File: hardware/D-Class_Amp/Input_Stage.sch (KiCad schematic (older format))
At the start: 19 parts, among them U201 LM324

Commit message: Added potentiometer to input gain stage, assigned all input footprints
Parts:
- removed R208: 39k, Resistor_SMD:R_0805_2012Metric_Pad1.20x1.40mm_HandSolder, symbol Device:R
- added RV201: 50k, Potentiometer_THT:Potentiometer_Vishay_T73YP_Vertical, symbol Device:R_POT
- added TP201: DC_Offset, TestPoint:TestPoint_THTPad_D2.0mm_Drill1.0mm, symbol Connector:TestPoint
- added TP202: Gain_Stage, TestPoint:TestPoint_THTPad_D2.0mm_Drill1.0mm, symbol Connector:TestPoint
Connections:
- net C_OUT: now also RV201.3
- net at C203.1, R201.2, R202.2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: now also TP201.1
- net at U201.10 (+): now also RV201.2, TP202.1
- no-connect marks 0 -> 1
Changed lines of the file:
@@
 	-1   0    0    -1
 $EndComp
-$Comp
-L Device:R R208
-U 1 1 610F6964
-P 3650 4400
-F 0 "R208" H 3580 4354 50  0000 R CNN
-F 1 "39k" H 3580 4445 50  0000 R CNN
-F 2 "Resistor_SMD:R_0805_2012Metric_Pad1.20x1.40mm_HandSolder" V 3580 4400 50  0001 C CNN
-F 3 "~" H 3650 4400 50  0001 C CNN
-	1    3650 4400
-	-1   0    0    -1
-$EndComp
-Wire Wire Line
-	3650 4600 3650 4550
 Connection ~ 3650 4600
 Wire Wire Line
 	3650 4600 3750 4600
-Wire Wire Line
-	3650 4250 3650 4200
-Wire Wire Line
-	3650 4200 2950 4200
 Wire Wire Line
 	2950 4200 2950 4500
@@
 $EndComp
 Wire Wire Line
-	2250 3200 2600 3200
+	2250 3200 2550 3200
+$Comp
+L Device:R_POT RV201
+U 1 1 61134898
+P 3650 4400
+F 0 "RV201" H 3580 4446 50  0000 R CNN
+F 1 "50k" H 3580 4355 50  0000 R CNN
+F 2 "Potentiometer_THT:Potentiometer_Vishay_T73YP_Vertical" H 3650 4400 50  0001 C CNN
+F 3 "~" H 3650 4400 50  0001 C CNN
+	1    3650 4400
+	1    0    0    -1
+$EndComp
+Wire Wire Line
+	3650 4600 3650 4550
+NoConn ~ 3650 4250
+Wire Wire Line
+	3850 4200 3850 4400
+Wire Wire Line
+	3850 4400 3800 4400
+Wire Wire Line
+	2950 4200 3850 4200
+$Comp
+L Connector:TestPoint TP202
+U 1 1 61142C7C
+P 3850 4150
+F 0 "TP202" H 3908 4268 50  0000 L CNN
+F 1 "Gain_Stage" H 3908 4177 50  0000 L CNN
+F 2 "TestPoint:TestPoint_THTPad_D2.0mm_Drill1.0mm" H 4050 4150 50  0001 C CNN
+F 3 "~" H 4050 4150 50  0001 C CNN
+	1    3850 4150
+	1    0    0    -1
+$EndComp
+Wire Wire Line
+	3850 4200 3850 4150
+Connection ~ 3850 4200
+$Comp
+L Connector:TestPoint TP201
+U 1 1 611488F4
+P 2550 2900
+F 0 "TP201" H 2608 3018 50  0000 L CNN
+F 1 "DC_Offset" H 2600 3100 50  0000 L CNN
+F 2 "TestPoint:TestPoint_THTPad_D2.0mm_Drill1.0mm" H 2750 2900 50  0001 C CNN
+F 3 "~" H 2750 2900 50  0001 C CNN
+	1    2550 2900
+	1    0    0    -1
+$EndComp
+Wire Wire Line
+	2550 2900 2550 3200
+Connection ~ 2550 3200
+Wire Wire Line
+	2550 3200 2600 3200
 $EndSCHEMATC

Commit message: Started input stage layout
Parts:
- R201, R206: footprint (none) -> Resistor_SMD:R_0805_2012Metric_Pad1.20x1.40mm_HandSolder
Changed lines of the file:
@@
 F 0 "R206" H 2180 3446 50  0000 R CNN
 F 1 "100k" H 2180 3355 50  0000 R CNN
-F 2 "" V 2180 3400 50  0001 C CNN
+F 2 "Resistor_SMD:R_0805_2012Metric_Pad1.20x1.40mm_HandSolder" V 2180 3400 50  0001 C CNN
 F 3 "~" H 2250 3400 50  0001 C CNN
 	1    2250 3400
@@
 F 0 "R201" H 2180 3046 50  0000 R CNN
 F 1 "100k" H 2180 2955 50  0000 R CNN
-F 2 "" V 2180 3000 50  0001 C CNN
+F 2 "Resistor_SMD:R_0805_2012Metric_Pad1.20x1.40mm_HandSolder" V 2180 3000 50  0001 C CNN
 F 3 "~" H 2250 3000 50  0001 C CNN
 	1    2250 3000

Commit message: Updated and fixed the input filter schematic
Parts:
- removed R206: 100k, Resistor_SMD:R_0805_2012Metric_Pad1.20x1.40mm_HandSolder, symbol Device:R
- added JP1: Filter_Bypass, Jumper:SolderJumper-2_P1.3mm_Open_TrianglePad1.0x1.5mm, symbol Jumper:SolderJumper_2_Open
- C201: value 100n -> 120n
- C202: value 100n -> 750n
- C207: value 100n -> 2.2u
- C208: value 100n -> 1.2u
- R202: value 5.6k -> 4.3k
- R203: value 8.2k -> 5.6k
- R204: value 5.6k -> 1.5k
- R205: value 8.2k -> 2.4k
- R210: value 8.2k -> 15k
- RV201: value 50k -> 20k
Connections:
- net +2V5: now also R201.1
- net +5V: no longer R201.1
- net A_OUT: now also U201.2 (-); no longer U201.3 (+)
- net B_OUT: now also U201.10 (+), U201.6 (-); no longer U201.5 (+), U201.9 (-)
- net C_OUT: now also JP1.2 (B)
- net FILT_OUT: now also U201.13 (-), JP1.1 (A); no longer U201.12 (+)
- net at C204.2, R203.1: now also U201.3 (+); no longer U201.2 (-)
- net at C205.2, R205.1: now also U201.5 (+); no longer U201.6 (-)
- net at RV201.2, TP202.1: now also U201.9 (-); no longer U201.10 (+)
- net at C208.1, R210.2: now also U201.12 (+); no longer U201.13 (-)
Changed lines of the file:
@@
 P 2750 3200
 F 0 "R202" V 2543 3200 50  0000 C CNN
-F 1 "5.6k" V 2634 3200 50  0000 C CNN
+F 1 "4.3k" V 2634 3200 50  0000 C CNN
 F 2 "Resistor_SMD:R_0805_2012Metric_Pad1.20x1.40mm_HandSolder" V 2680 3200 50  0001 C CNN
 F 3 "~" H 2750 3200 50  0001 C CNN
@@
 P 3150 3200
 F 0 "R203" V 2943 3200 50  0000 C CNN
-F 1 "8.2k" V 3034 3200 50  0000 C CNN
+F 1 "5.6k" V 3034 3200 50  0000 C CNN
 F 2 "Resistor_SMD:R_0805_2012Metric_Pad1.20x1.40mm_HandSolder" V 3080 3200 50  0001 C CNN
 F 3 "~" H 3150 3200 50  0001 C CNN
@@
 P 3150 2800
 F 0 "C201" V 2898 2800 50  0000 C CNN
-F 1 "100n" V 2989 2800 50  0000 C CNN
+F 1 "120n" V 2989 2800 50  0000 C CNN
 F 2 "Capacitor_SMD:C_0805_2012Metric_Pad1.18x1.45mm_HandSolder" H 3188 2650 50  0001 C CNN
 F 3 "~" H 3150 2800 50  0001 C CNN
@@
 P 5300 3200
 F 0 "R204" V 5093 3200 50  0000 C CNN
-F 1 "5.6k" V 5184 3200 50  0000 C CNN
+F 1 "1.5k" V 5184 3200 50  0000 C CNN
 F 2 "Resistor_SMD:R_0805_2012Metric_Pad1.20x1.40mm_HandSolder" V 5230 3200 50  0001 C CNN
 F 3 "~" H 5300 3200 50  0001 C CNN
@@
 P 5700 3200
 F 0 "R205" V 5493 3200 50  0000 C CNN
-F 1 "8.2k" V 5584 3200 50  0000 C CNN
+F 1 "2.4k" V 5584 3200 50  0000 C CNN
 F 2 "Resistor_SMD:R_0805_2012Metric_Pad1.20x1.40mm_HandSolder" V 5630 3200 50  0001 C CNN
 F 3 "~" H 5700 3200 50  0001 C CNN
@@
 P 5700 2800
 F 0 "C202" V 5448 2800 50  0000 C CNN
-F 1 "100n" V 5539 2800 50  0000 C CNN
+F 1 "750n" V 5539 2800 50  0000 C CNN
 F 2 "Capacitor_SMD:C_0805_2012Metric_Pad1.18x1.45mm_HandSolder" H 5738 2650 50  0001 C CNN
 F 3 "~" H 5700 2800 50  0001 C CNN
@@
 P 5900 4850
 F 0 "R210" H 5830 4804 50  0000 R CNN
-F 1 "8.2k" H 5830 4895 50  0000 R CNN
+F 1 "15k" H 5830 4895 50  0000 R CNN
 F 2 "Resistor_SMD:R_0805_2012Metric_Pad1.20x1.40mm_HandSolder" V 5830 4850 50  0001 C CNN
 F 3 "~" H 5900 4850 50  0001 C CNN
@@
 P 5700 4650
 F 0 "C208" V 5448 4650 50  0000 C CNN
-F 1 "100n" V 5539 4650 50  0000 C CNN
+F 1 "1.2u" V 5539 4650 50  0000 C CNN
 F 2 "Capacitor_SMD:C_0805_2012Metric_Pad1.18x1.45mm_HandSolder" H 5738 4500 50  0001 C CNN
 F 3 "~" H 5700 4650 50  0001 C CNN
@@
 P 5300 4650
 F 0 "C207" V 5048 4650 50  0000 C CNN
-F 1 "100n" V 5139 4650 50  0000 C CNN
+F 1 "2.2u" V 5139 4650 50  0000 C CNN
 F 2 "Capacitor_SMD:C_0805_2012Metric_Pad1.18x1.45mm_HandSolder" H 5338 4500 50  0001 C CNN
 F 3 "~" H 5300 4650 50  0001 C CNN
@@
 P 3700 3100
 F 0 "U201" H 3700 3100 50  0000 C CNN
-F 1 "LM324" H 3700 2850 50  0000 C CNN
+F 1 "LM324" H 3700 3350 50  0000 C CNN
 F 2 "Package_SO:SOIC-14_3.9x8.7mm_P1.27mm" H 3650 3200 50  0001 C CNN
 F 3 "http://www.ti.com/lit/ds/symlink/lm2902-n.pdf" H 3750 3300 50  0001 C CNN
 	1    3700 3100
-	1    0    0    -1
+	1    0    0    1
 $EndComp
 $Comp
@@
 P 6250 3100
 F 0 "U201" H 6250 3100 50  0000 C CNN
-F 1 "LM324" H 6250 2850 50  0000 C CNN
+F 1 "LM324" H 6250 3350 50  0000 C CNN
 F 2 "Package_SO:SOIC-14_3.9x8.7mm_P1.27mm" H 6200 3200 50  0001 C CNN
 F 3 "http://www.ti.com/lit/ds/symlink/lm2902-n.pdf" H 6300 3300 50  0001 C CNN
 	2    6250 3100
-	1    0    0    -1
+	1    0    0    1
 $EndComp
 $Comp
@@
 P 3300 4600
 F 0 "U201" H 3300 4600 50  0000 C CNN
-F 1 "LM324" H 3300 4350 50  0000 C CNN
+F 1 "LM324" H 3300 4850 50  0000 C CNN
 F 2 "Package_SO:SOIC-14_3.9x8.7mm_P1.27mm" H 3250 4700 50  0001 C CNN
 F 3 "http://www.ti.com/lit/ds/symlink/lm2902-n.pdf" H 3350 4800 50  0001 C CNN
 	3    3300 4600
-	1    0    0    -1
+	1    0    0    1
 $EndComp
 $Comp
@@
 P 6250 4550
 F 0 "U201" H 6250 4550 50  0000 C CNN
-F 1 "LM324" H 6250 4300 50  0000 C CNN
+F 1 "LM324" H 6250 4800 50  0000 C CNN
 F 2 "Package_SO:SOIC-14_3.9x8.7mm_P1.27mm" H 6200 4650 50  0001 C CNN
 F 3 "http://www.ti.com/lit/ds/symlink/lm2902-n.pdf" H 6300 4750 50  0001 C CNN
 	4    6250 4550
-	1    0    0    -1
+	1    0    0    1
 $EndComp
 $Comp
@@
 $EndComp
 $Comp
-L power:GNDS #PWR0202
-U 1 1 610B63BB
-P 2250 3550
-F 0 "#PWR0202" H 2250 3300 50  0001 C CNN
-F 1 "GNDS" H 2255 3377 50  0000 C CNN
-F 2 "" H 2250 3550 50  0001 C CNN
-F 3 "" H 2250 3550 50  0001 C CNN
-	1    2250 3550
-	1    0    0    -1
-$EndComp
-$Comp
-L power:+5V #PWR0201
-U 1 1 610B76DD
-P 2250 2850
-F 0 "#PWR0201" H 2250 2700 50  0001 C CNN
-F 1 "+5V" H 2265 3023 50  0000 C CNN
-F 2 "" H 2250 2850 50  0001 C CNN
-F 3 "" H 2250 2850 50  0001 C CNN
-	1    2250 2850
-	1    0    0    -1
-$EndComp
-$Comp
-L Device:R R206
-U 1 1 610B8ECE
-P 2250 3400
-F 0 "R206" H 2180 3446 50  0000 R CNN
-F 1 "100k" H 2180 3355 50  0000 R CNN
-F 2 "Resistor_SMD:R_0805_2012Metric_Pad1.20x1.40mm_HandSolder" V 2180 3400 50  0001 C CNN
-F 3 "~" H 2250 3400 50  0001 C CNN
-	1    2250 3400
-	-1   0    0    -1
-$EndComp
-$Comp
 L Device:R R201
 U 1 1 610BCA88
@@
 Connection ~ 2250 3200
 Wire Wire Line
-	2250 3200 2250 3250
-Wire Wire Line
 	3600 4600 3650 4600
 $Comp
@@
 P 3650 4400
 F 0 "RV201" H 3580 4446 50  0000 R CNN
-F 1 "50k" H 3580 4355 50  0000 R CNN
+F 1 "20k" H 3580 4355 50  0000 R CNN
 F 2 "Potentiometer_THT:Potentiometer_Vishay_T73YP_Vertical" H 3650 4400 50  0001 C CNN
 F 3 "~" H 3650 4400 50  0001 C CNN
@@
 Wire Wire Line
 	2550 3200 2600 3200
+$Comp
+L power:+2V5 #PWR0110
+U 1 1 611434AC
+P 2250 2850
+F 0 "#PWR0110" H 2250 2700 50  0001 C CNN
+F 1 "+2V5" H 2265 3023 50  0000 C CNN
+F 2 "" H 2250 2850 50  0001 C CNN
+F 3 "" H 2250 2850 50  0001 C CNN
+	1    2250 2850
+	1    0    0    -1
+$EndComp
+Text Label 6600 5000 3    50   ~ 0
+C_OUT
+$Comp
+L Jumper:SolderJumper_2_Open JP1
+U 1 1 6115E400
+P 6600 4750
+F 0 "JP1" V 6554 4818 50  0000 L CNN
+F 1 "Filter_Bypass" V 6645 4818 50  0000 L CNN
+F 2 "Jumper:SolderJumper-2_P1.3mm_Open_TrianglePad1.0x1.5mm" H 6600 4750 50  0001 C CNN
+F 3 "~" H 6600 4750 50  0001 C CNN
+	1    6600 4750
+	0    1    1    0
+$EndComp
+Wire Wire Line
+	6600 5000 6600 4900
+Wire Wire Line
+	6600 4600 6600 4550
 $EndSCHEMATC

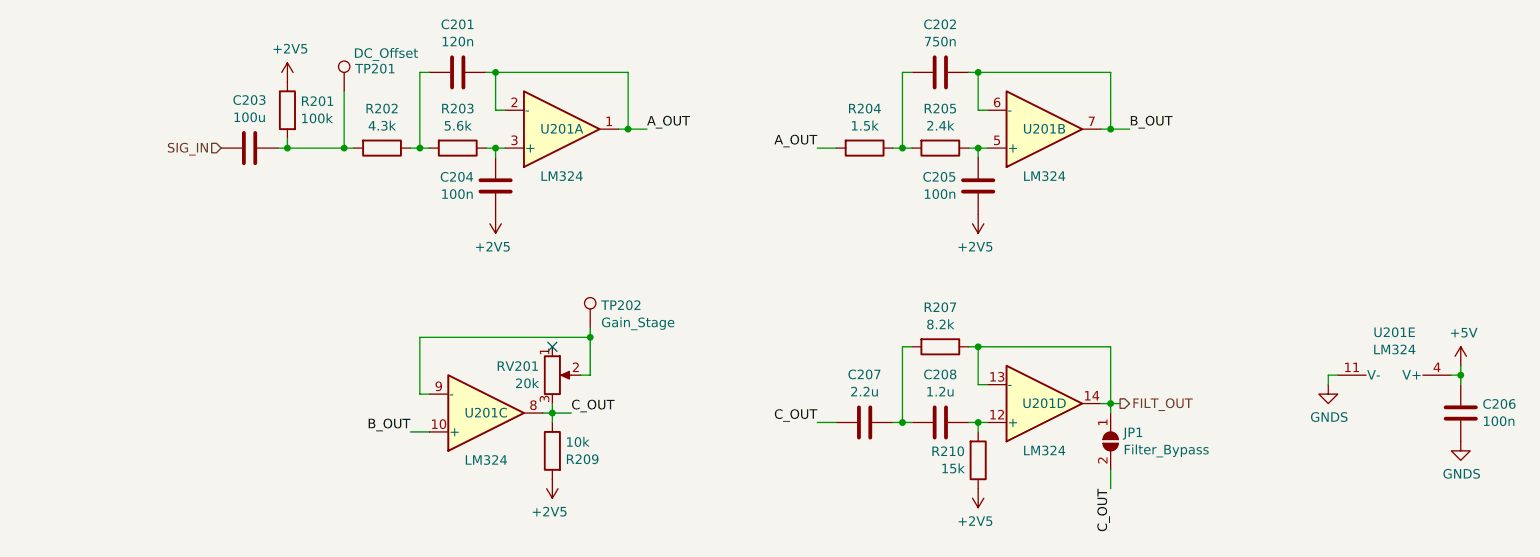
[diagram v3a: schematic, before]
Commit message: added pricing and and part numbers to all components
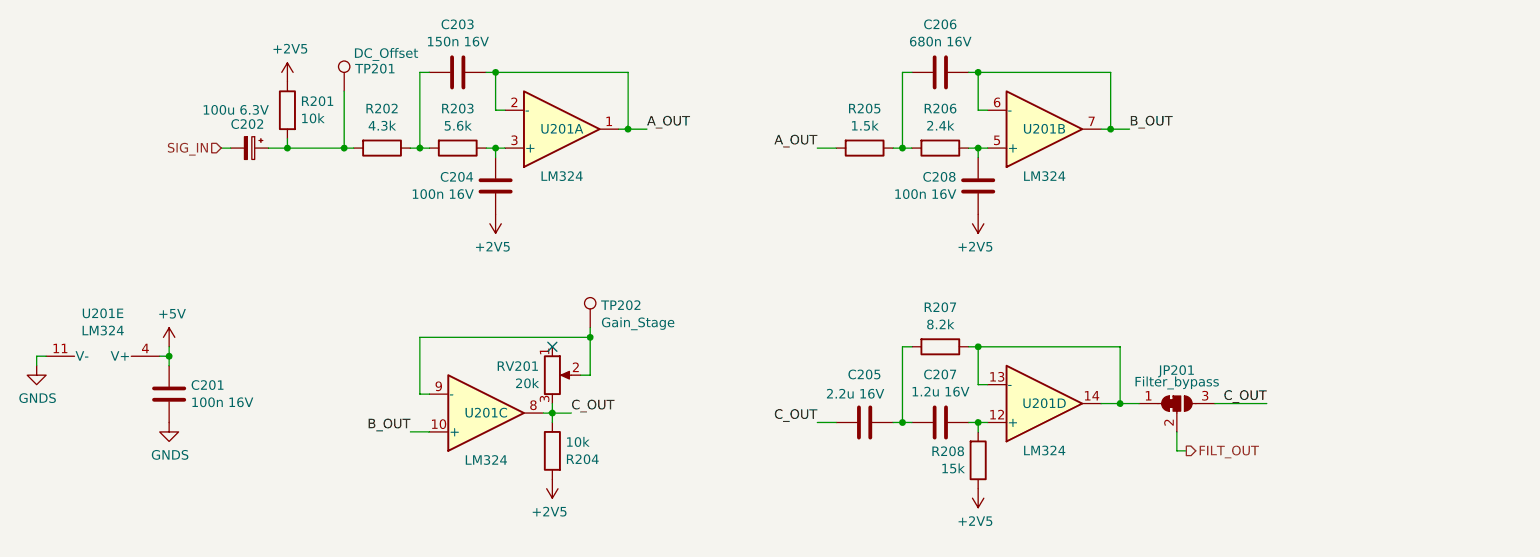
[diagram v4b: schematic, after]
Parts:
- removed C203: 100u, Capacitor_SMD:C_0805_2012Metric_Pad1.18x1.45mm_HandSolder, symbol Device:C
- removed JP1: Filter_Bypass, Jumper:SolderJumper-2_P1.3mm_Open_TrianglePad1.0x1.5mm, symbol Jumper:SolderJumper_2_Open
- added C202: 100u 6.3V, Capacitor_SMD:CP_Elec_4x5.4, symbol Device:CP_Small
- added JP201: Filter_bypass, Jumper:SolderJumper-3_P1.3mm_Bridged12_RoundedPad1.0x1.5mm_NumberLabels, symbol Jumper:SolderJumper_3_Bridged12
- C201: renamed from C206; value 100n -> 100n 16V; DigiKey Price (none) -> 0.16; Part Number (none) -> 885012207045
- C203: renamed from C201; value 120n -> 150n 16V; DigiKey Price (none) -> 0.16; Part Number (none) -> CL21B154KOANNNC
- C204: value 100n -> 100n 16V; DigiKey Price (none) -> 0.16; Part Number (none) -> 885012207045
- C205: renamed from C207; value 2.2u -> 2.2u 16V; DigiKey Price (none) -> 0.26; Part Number (none) -> L21A225KOFNNNE
- C206: renamed from C202; value 750n -> 680n 16V; DigiKey Price (none) -> 0.16; Part Number (none) -> CL21B684KOFNNNG
- C207: renamed from C208; value 1.2u -> 1.2u 16V; DigiKey Price (none) -> 0.67; Part Number (none) -> C0805C125K4PAC7800
- C208: renamed from C205; value 100n -> 100n 16V; DigiKey Price (none) -> 0.16; Part Number (none) -> 885012207045
- R201: value 100k -> 10k; DigiKey Price (none) -> 0.16; Part Number (none) -> RC0805JR-0710KL
- R202: DigiKey Price (none) -> 0.16; Part Number (none) -> RC0805JR-074K3L
- R203: DigiKey Price (none) -> 0.16; Part Number (none) -> RC0805JR-075K6L
- R204: renamed from R209; DigiKey Price (none) -> 0.16; Part Number (none) -> RC0805JR-0710KL
- R205: renamed from R204; DigiKey Price (none) -> 0.16; Part Number (none) -> CRCW08051K50FKEAC
- R206: renamed from R205; DigiKey Price (none) -> 0.16; Part Number (none) -> ERA-6AED242V
- R207: DigiKey Price (none) -> 0.16; Part Number (none) -> RC0805JR-078K2L
- R208: renamed from R210; DigiKey Price (none) -> 0.16; Part Number (none) -> RC0805JR-0715KL
- RV201: DigiKey Price (none) -> 0.16; Part Number (none) -> ERJ-6ENF2002V
- U201: DigiKey Price (none) -> 0.62; Part Number (none) -> LM324DR
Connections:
- net C_OUT: now also JP201.3 (B)
- net FILT_OUT: now also JP201.2 (C); no longer R207.1, U201.13 (-), U201.14
- net SIG_IN: now also C202.2
- net at R201.2, R202.2, TP201.1: now also C202.1
- new net: JP201.1 (A), R207.1, U201.13 (-), U201.14
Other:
- moved on the sheet: C201, U201E

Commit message: placed and routed all components, fixed the MOSFET footprints, and added all 3D models.
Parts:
- TP201, TP202: footprint TestPoint:TestPoint_THTPad_D2.0mm_Drill1.0mm -> TestPoint:TestPoint_THTPad_D1.0mm_Drill0.5mm
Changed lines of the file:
@@
 F 0 "TP201" H 2608 3018 50  0000 L CNN
 F 1 "DC_Offset" H 2600 3100 50  0000 L CNN
-F 2 "TestPoint:TestPoint_THTPad_D2.0mm_Drill1.0mm" H 2750 2900 50  0001 C CNN
+F 2 "TestPoint:TestPoint_THTPad_D1.0mm_Drill0.5mm" H 2750 2900 50  0001 C CNN
 F 3 "~" H 2750 2900 50  0001 C CNN
 	1    2550 2900
@@
 F 0 "TP202" H 3908 4268 50  0000 L CNN
 F 1 "Gain_Stage" H 3908 4177 50  0000 L CNN
-F 2 "TestPoint:TestPoint_THTPad_D2.0mm_Drill1.0mm" H 4050 4150 50  0001 C CNN
+F 2 "TestPoint:TestPoint_THTPad_D1.0mm_Drill0.5mm" H 4050 4150 50  0001 C CNN
 F 3 "~" H 4050 4150 50  0001 C CNN
 	1    3850 4150

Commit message: PCB done POG
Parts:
- RV201: DigiKey Price 0.16 -> 1.25; Part Number ERJ-6ENF2002V -> CT6EP203
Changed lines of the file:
@@
 F 1 "20k" H 3580 4355 50  0000 R CNN
 F 2 "Potentiometer_THT:Potentiometer_Vishay_T73YP_Vertical" H 3650 4400 50  0001 C CNN
-F 3 "~" H 3650 4400 50  0001 C CNN
-F 4 "0.16" H 3650 4400 50  0001 C CNN "DigiKey Price"
-F 5 "ERJ-6ENF2002V" H 3650 4400 50  0001 C CNN "Part Number"
+F 3 "https://www.nidec-copal-electronics.com/e/catalog/trimmer/ct-6.pdf" H 3650 4400 50  0001 C CNN
+F 4 "1.25" H 3650 4400 50  0001 C CNN "DigiKey Price"
+F 5 "CT6EP203" H 3650 4400 50  0001 C CNN "Part Number"
 	1    3650 4400
 	1    0    0    -1

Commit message: readded art and regen bom
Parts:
- C202: symbol Device:CP_Small -> D-Class_Amp-rescue:CP_Small-Device
- RV201: symbol Device:R_POT -> D-Class_Amp-rescue:R_POT-Device
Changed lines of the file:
@@
 	2250 3200 2550 3200
 $Comp
-L Device:R_POT RV201
+L D-Class_Amp-rescue:R_POT-Device RV201
 U 1 1 61134898
 P 3650 4400
@@
 	7425 4550 7150 4550
 $Comp
-L Device:CP_Small C?
+L D-Class_Amp-rescue:CP_Small-Device C?
 U 1 1 6134BD3A
 P 2050 3200
